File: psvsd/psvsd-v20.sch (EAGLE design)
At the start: 26 parts, among them U1 GL823(A)OG, U2 74AUP1G74DC, U3 LP3996_DSC_10

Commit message: Added USB trace clearance recommendations from GL823 design docs
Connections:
- net GND: no longer U$1G$1.GND@22
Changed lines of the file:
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@@
 <?xml version="1.0" encoding="utf-8"?>
 <!DOCTYPE eagle SYSTEM "eagle.dtd">
-<eagle version="8.2.0">
+<eagle version="8.2.2">
 <drawing>
 <settings>
@@
 <class number="0" name="default" width="0" drill="0">
 </class>
+<class number="1" name="USB" width="0" drill="0">
+</class>
+<class number="2" name="Clock/HS" width="0" drill="0">
+<clearance class="1" value="1.27"/>
+</class>
+<class number="3" name="GND" width="0" drill="0">
+<clearance class="1" value="0.508"/>
+</class>
 </classes>
 <parts>
@@
 </segment>
 </net>
-<net name="GND" class="0">
+<net name="GND" class="3">
 <segment>
 <pinref part="U$1" gate="G$1" pin="GND@4"/>
@@
 <wire x1="-35.56" y1="-17.78" x2="-38.1" y2="-17.78" width="0.1524" layer="91"/>
 <label x="-40.64" y="-17.78" size="1.778" layer="95"/>
-</segment>
-<segment>
-<pinref part="U$1" gate="G$1" pin="GND@22"/>
-<wire x1="86.36" y1="5.08" x2="93.98" y2="5.08" width="0.1524" layer="91"/>
-<label x="86.36" y="5.08" size="1.778" layer="95"/>
 </segment>
 <segment>
@@
 </segment>
 </net>
-<net name="USB_N" class="0">
+<net name="USB_N" class="1">
 <segment>
 <pinref part="U$1" gate="G$1" pin="USB_D-"/>
@@
 </segment>
 </net>
-<net name="USB_P" class="0">
+<net name="USB_P" class="1">
 <segment>
 <pinref part="U$1" gate="G$1" pin="USB_D+"/>
@@
 </segment>
 </net>
-<net name="SD_CLK" class="0">
+<net name="SD_CLK" class="2">
 <segment>
 <pinref part="U1" gate="G$1" pin="SD_CLK"/>
@@
 </segment>
 </net>
-<net name="SD_D0" class="0">
+<net name="SD_D0" class="2">
 <segment>
 <pinref part="U1" gate="G$1" pin="SD_D0"/>
@@
 </segment>
 </net>
-<net name="SD_D1" class="0">
+<net name="SD_D1" class="3">
 <segment>
 <pinref part="U1" gate="G$1" pin="SD_D1"/>
@@
 </segment>
 </net>
-<net name="SD_D2" class="0">
+<net name="SD_D2" class="2">
 <segment>
 <pinref part="U1" gate="G$1" pin="SD_D2"/>
@@
 </segment>
 </net>
-<net name="SD_D3" class="0">
+<net name="SD_D3" class="2">
 <segment>
 <pinref part="U1" gate="G$1" pin="SD_D3"/>
@@
 </busses>
 <nets>
-<net name="GND" class="0">
+<net name="GND" class="3">
 <segment>
 <pinref part="C1" gate="G$1" pin="2"/>

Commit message: Changed bypass value for DVDD2 and added a new ferrite bead to AVDD
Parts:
- added FB2: BLM15HB121SN1, inductors:BLM15HB121SN1
- C3: value 0.1uF -> 10uF
- C8: value ? -> 0.1uF
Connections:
- new net AVDD: FB2.2, U1.AVDD
- net VDD33: now also FB2.1; no longer U1.AVDD
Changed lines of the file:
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@@
 <?xml version="1.0" encoding="utf-8"?>
 <!DOCTYPE eagle SYSTEM "eagle.dtd">
-<eagle version="8.2.2">
+<eagle version="8.2.0">
 <drawing>
 <settings>
@@
 <layers>
 <layer number="1" name="Top" color="4" fill="1" visible="no" active="no"/>
+<layer number="2" name="Route2" color="1" fill="3" visible="no" active="no"/>
+<layer number="3" name="Route3" color="4" fill="3" visible="no" active="no"/>
+<layer number="4" name="Route4" color="1" fill="4" visible="no" active="no"/>
+<layer number="5" name="Route5" color="4" fill="4" visible="no" active="no"/>
+<layer number="6" name="Route6" color="1" fill="8" visible="no" active="no"/>
+<layer number="7" name="Route7" color="4" fill="8" visible="no" active="no"/>
+<layer number="8" name="Route8" color="1" fill="2" visible="no" active="no"/>
+<layer number="9" name="Route9" color="4" fill="2" visible="no" active="no"/>
+<layer number="10" name="Route10" color="1" fill="7" visible="no" active="no"/>
+<layer number="11" name="Route11" color="4" fill="7" visible="no" active="no"/>
+<layer number="12" name="Route12" color="1" fill="5" visible="no" active="no"/>
+<layer number="13" name="Route13" color="4" fill="5" visible="no" active="no"/>
+<layer number="14" name="Route14" color="1" fill="6" visible="no" active="no"/>
+<layer number="15" name="Route15" color="4" fill="6" visible="no" active="no"/>
 <layer number="16" name="Bottom" color="1" fill="1" visible="no" active="no"/>
 <layer number="17" name="Pads" color="2" fill="1" visible="no" active="no"/>
@@
 <part name="SD1" library="Seeed-Connector" library_urn="urn:adsk.eagle:library:478" deviceset="MICRO-SD-CARD-SOCKET-9P(ST-TF-003A)" device="" value="ST-TF-003A"/>
 <part name="U1" library="GL823" deviceset="GL823(A)" device="OG"/>
-<part name="C3" library="rcl" library_urn="urn:adsk.eagle:library:334" deviceset="C-EU" device="C0402" value="0.1uF"/>
+<part name="C3" library="rcl" library_urn="urn:adsk.eagle:library:334" deviceset="C-EU" device="C0402" value="10uF"/>
 <part name="C4" library="rcl" library_urn="urn:adsk.eagle:library:334" deviceset="C-EU" device="C0402" value="0.1uF"/>
 <part name="GND2" library="supply1" library_urn="urn:adsk.eagle:library:371" deviceset="GND" device=""/>
@@
 <part name="C7" library="rcl" library_urn="urn:adsk.eagle:library:334" deviceset="C-EU" device="C0402" value="0.1uF"/>
 <part name="GND9" library="supply1" library_urn="urn:adsk.eagle:library:371" deviceset="GND" device=""/>
-<part name="C8" library="rcl" library_urn="urn:adsk.eagle:library:334" deviceset="C-EU" device="C0402" value="?"/>
+<part name="C8" library="rcl" library_urn="urn:adsk.eagle:library:334" deviceset="C-EU" device="C0402" value="0.1uF"/>
+<part name="FB2" library="inductors" library_urn="urn:adsk.eagle:library:243" deviceset="BLM15H" device="" technology="B121SN1" value=""/>
 </parts>
 <sheets>
@@
 <instance part="GND9" gate="1" x="-35.56" y="-43.18"/>
 <instance part="C8" gate="G$1" x="-43.18" y="-33.02"/>
+<instance part="FB2" gate="G$1" x="-104.14" y="-10.16"/>
 </instances>
 <busses>
@@
 <wire x1="-114.3" y1="-10.16" x2="-114.3" y2="-7.62" width="0.1524" layer="91"/>
 <junction x="-114.3" y="-7.62"/>
-<pinref part="U1" gate="G$1" pin="AVDD"/>
-<wire x1="-114.3" y1="-10.16" x2="-88.9" y2="-10.16" width="0.1524" layer="91"/>
+<wire x1="-114.3" y1="-10.16" x2="-109.22" y2="-10.16" width="0.1524" layer="91"/>
 <junction x="-114.3" y="-10.16"/>
+<pinref part="FB2" gate="G$1" pin="1"/>
 </segment>
 </net>
@@
 </segment>
 </net>
+<net name="AVDD" class="0">
+<segment>
+<pinref part="U1" gate="G$1" pin="AVDD"/>
+<pinref part="FB2" gate="G$1" pin="2"/>
+<wire x1="-99.06" y1="-10.16" x2="-88.9" y2="-10.16" width="0.1524" layer="91"/>
+</segment>
+</net>

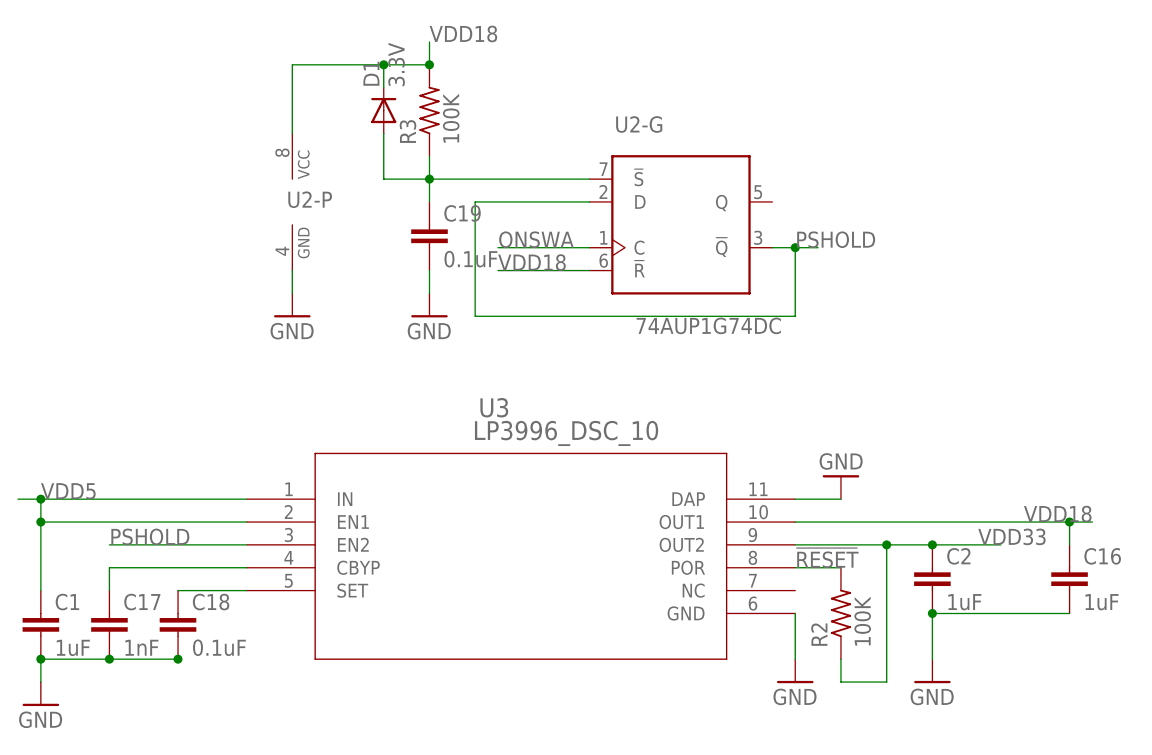
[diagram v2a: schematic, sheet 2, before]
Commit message: Added RC delay to power circuit
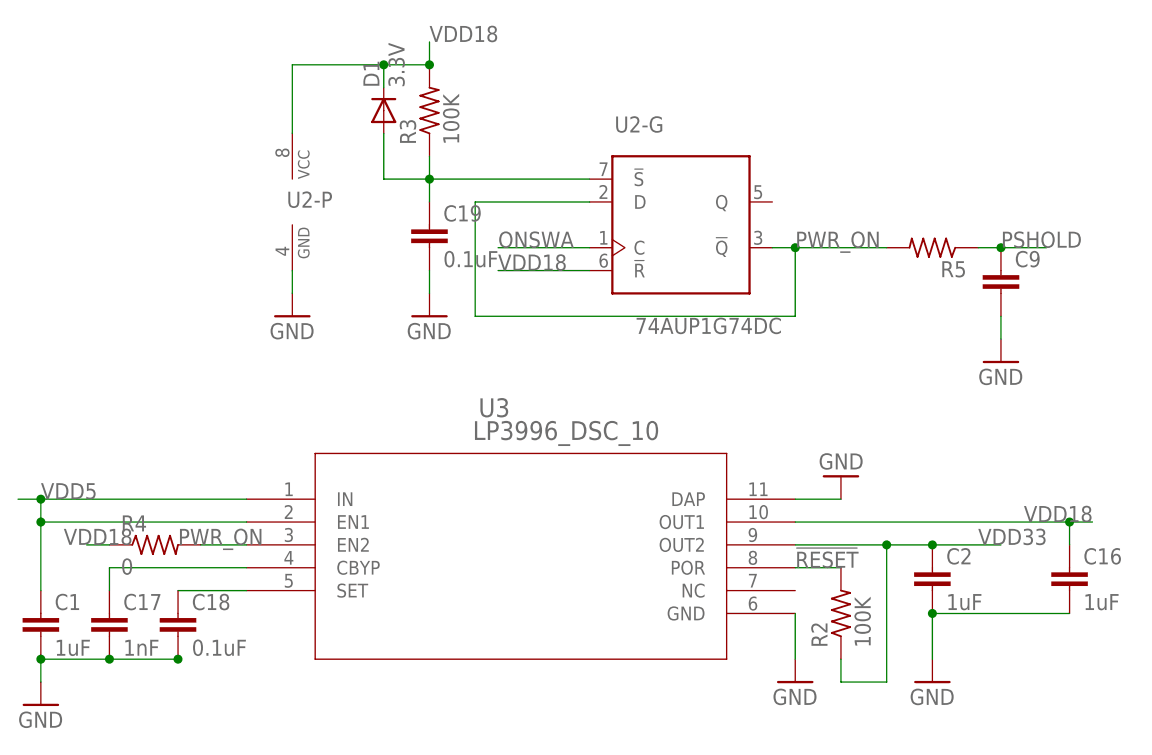
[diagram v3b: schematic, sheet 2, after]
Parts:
- added C9: (no value), rcl:C-EUC0402
- added R4: 0, rcl:R-US_R0402
- added R5: (no value), rcl:R-US_R0603
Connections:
- new net PWR_ON: R4.2, R5.2, U2-G.!Q, U2-G.D, U3.EN2
- net GND: now also C9.2
- net PSHOLD: now also C9.1, R5.1; no longer U2-G.!Q, U2-G.D, U3.EN2
- net VDD18: now also R4.1
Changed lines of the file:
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@@
 <part name="C8" library="rcl" library_urn="urn:adsk.eagle:library:334" deviceset="C-EU" device="C0402" value="0.1uF"/>
 <part name="FB2" library="inductors" library_urn="urn:adsk.eagle:library:243" deviceset="BLM15H" device="" technology="B121SN1" value=""/>
+<part name="R4" library="rcl" library_urn="urn:adsk.eagle:library:334" deviceset="R-US_" device="R0402" value="0"/>
+<part name="C9" library="rcl" library_urn="urn:adsk.eagle:library:334" deviceset="C-EU" device="C0402"/>
+<part name="R5" library="rcl" library_urn="urn:adsk.eagle:library:334" deviceset="R-US_" device="R0603"/>
+<part name="GND10" library="supply1" library_urn="urn:adsk.eagle:library:371" deviceset="GND" device=""/>
 </parts>
 <sheets>
@@
 </segment>
 </net>
-<net name="PSHOLD" class="0">
-<segment>
-<pinref part="U$1" gate="G$1" pin="PSHOLD"/>
-<wire x1="17.78" y1="12.7" x2="5.08" y2="12.7" width="0.1524" layer="91"/>
-<label x="5.08" y="12.7" size="1.778" layer="95"/>
-</segment>
-</net>
 <net name="VDD33" class="0">
 <segment>
@@
 <pinref part="FB2" gate="G$1" pin="2"/>
 <wire x1="-99.06" y1="-10.16" x2="-88.9" y2="-10.16" width="0.1524" layer="91"/>
+</segment>
+</net>
+<net name="PSHOLD" class="0">
+<segment>
+<pinref part="U$1" gate="G$1" pin="PSHOLD"/>
+<wire x1="17.78" y1="12.7" x2="5.08" y2="12.7" width="0.1524" layer="91"/>
+<label x="5.08" y="12.7" size="1.778" layer="95"/>
 </segment>
 </net>
@@
 <instance part="GND18" gate="1" x="-10.16" y="73.66"/>
 <instance part="C17" gate="G$1" x="-30.48" y="40.64"/>
+<instance part="R4" gate="G$1" x="-25.4" y="48.26"/>
+<instance part="C9" gate="G$1" x="68.58" y="78.74"/>
+<instance part="R5" gate="G$1" x="60.96" y="81.28" rot="R180"/>
+<instance part="GND10" gate="1" x="68.58" y="68.58"/>
 </instances>
 <busses>
@@
 <pinref part="U2" gate="-P" pin="GND"/>
 <wire x1="-10.16" y1="76.2" x2="-10.16" y2="78.74" width="0.1524" layer="91"/>
+</segment>
+<segment>
+<pinref part="C9" gate="G$1" pin="2"/>
+<wire x1="68.58" y1="73.66" x2="68.58" y2="71.12" width="0.1524" layer="91"/>
+<pinref part="GND10" gate="1" pin="GND"/>
 </segment>
 </net>
@@
 <wire x1="22.86" y1="81.28" x2="12.7" y2="81.28" width="0.1524" layer="91"/>
 <label x="12.7" y="81.28" size="1.778" layer="95"/>
-</segment>
-</net>
-<net name="PSHOLD" class="0">
-<segment>
-<pinref part="U2" gate="-G" pin="!Q"/>
-<wire x1="43.18" y1="81.28" x2="45.72" y2="81.28" width="0.1524" layer="91"/>
-<wire x1="45.72" y1="81.28" x2="45.72" y2="73.66" width="0.1524" layer="91"/>
-<wire x1="45.72" y1="73.66" x2="10.16" y2="73.66" width="0.1524" layer="91"/>
-<wire x1="10.16" y1="73.66" x2="10.16" y2="86.36" width="0.1524" layer="91"/>
-<pinref part="U2" gate="-G" pin="D"/>
-<wire x1="10.16" y1="86.36" x2="22.86" y2="86.36" width="0.1524" layer="91"/>
-<wire x1="45.72" y1="81.28" x2="48.26" y2="81.28" width="0.1524" layer="91"/>
-<label x="45.72" y="81.28" size="1.778" layer="95"/>
-<junction x="45.72" y="81.28"/>
-</segment>
-<segment>
-<pinref part="U3" gate="A" pin="EN2"/>
-<wire x1="-15.24" y1="48.26" x2="-30.48" y2="48.26" width="0.1524" layer="91"/>
-<label x="-30.48" y="48.26" size="1.778" layer="95"/>
 </segment>
 </net>
@@
 <junction x="0" y="101.6"/>
 </segment>
+<segment>
+<pinref part="R4" gate="G$1" pin="1"/>
+<wire x1="-30.48" y1="48.26" x2="-33.02" y2="48.26" width="0.1524" layer="91"/>
+<label x="-35.56" y="48.26" size="1.778" layer="95"/>
+</segment>
 </net>
 <net name="CBYP" class="0">
@@
 </segment>
 </net>
+<net name="PWR_ON" class="0">
+<segment>
+<pinref part="U2" gate="-G" pin="!Q"/>
+<wire x1="43.18" y1="81.28" x2="45.72" y2="81.28" width="0.1524" layer="91"/>
+<wire x1="45.72" y1="81.28" x2="45.72" y2="73.66" width="0.1524" layer="91"/>
+<wire x1="45.72" y1="73.66" x2="10.16" y2="73.66" width="0.1524" layer="91"/>
+<wire x1="10.16" y1="73.66" x2="10.16" y2="86.36" width="0.1524" layer="91"/>
+<pinref part="U2" gate="-G" pin="D"/>
+<wire x1="10.16" y1="86.36" x2="22.86" y2="86.36" width="0.1524" layer="91"/>
+<label x="45.72" y="81.28" size="1.778" layer="95"/>
+<junction x="45.72" y="81.28"/>
+<pinref part="R5" gate="G$1" pin="2"/>
+<wire x1="45.72" y1="81.28" x2="55.88" y2="81.28" width="0.1524" layer="91"/>
+</segment>
+<segment>
+<pinref part="U3" gate="A" pin="EN2"/>
+<wire x1="-15.24" y1="48.26" x2="-20.32" y2="48.26" width="0.1524" layer="91"/>
+<label x="-22.86" y="48.26" size="1.778" layer="95"/>
+<pinref part="R4" gate="G$1" pin="2"/>
+</segment>
+</net>
+<net name="PSHOLD" class="0">
+<segment>
+<pinref part="R5" gate="G$1" pin="1"/>
+<pinref part="C9" gate="G$1" pin="1"/>
+<wire x1="66.04" y1="81.28" x2="68.58" y2="81.28" width="0.1524" layer="91"/>
+<wire x1="68.58" y1="81.28" x2="73.66" y2="81.28" width="0.1524" layer="91"/>
+<junction x="68.58" y="81.28"/>
+<label x="68.58" y="81.28" size="1.778" layer="95"/>
+</segment>
+</net>
